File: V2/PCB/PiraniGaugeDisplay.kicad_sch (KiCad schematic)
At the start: 70 parts, among them J101 AuxIN, J102 Conn_02x03_Odd_Even, J103 RJ45, U101 AMS1117-3.3, U102 SN75176AD, U103 LM2596S-5, U104 ESP32-S3-WROOM-1(N16R2)

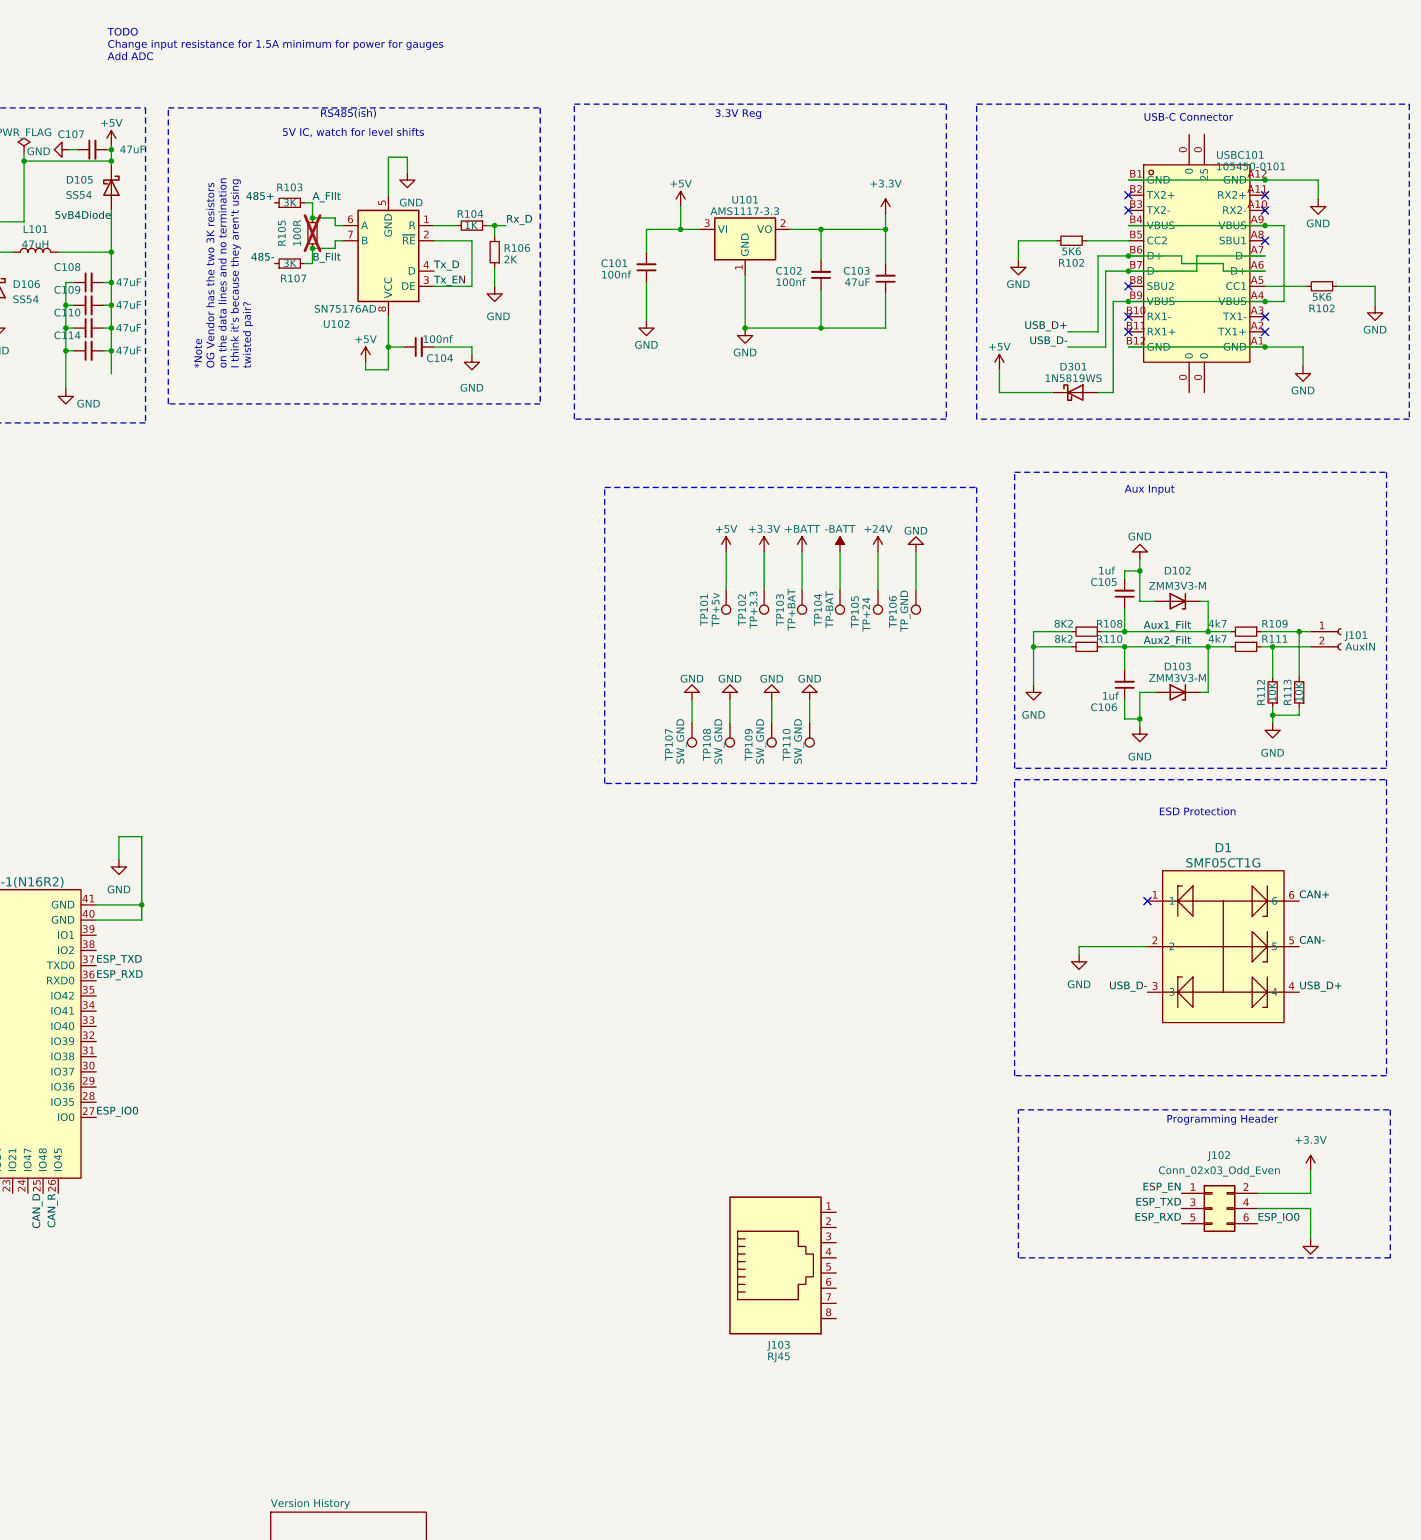
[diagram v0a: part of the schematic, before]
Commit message: Added buttons
Added boot/reset buttons to PCB
Should probably add some extras just for future expansion
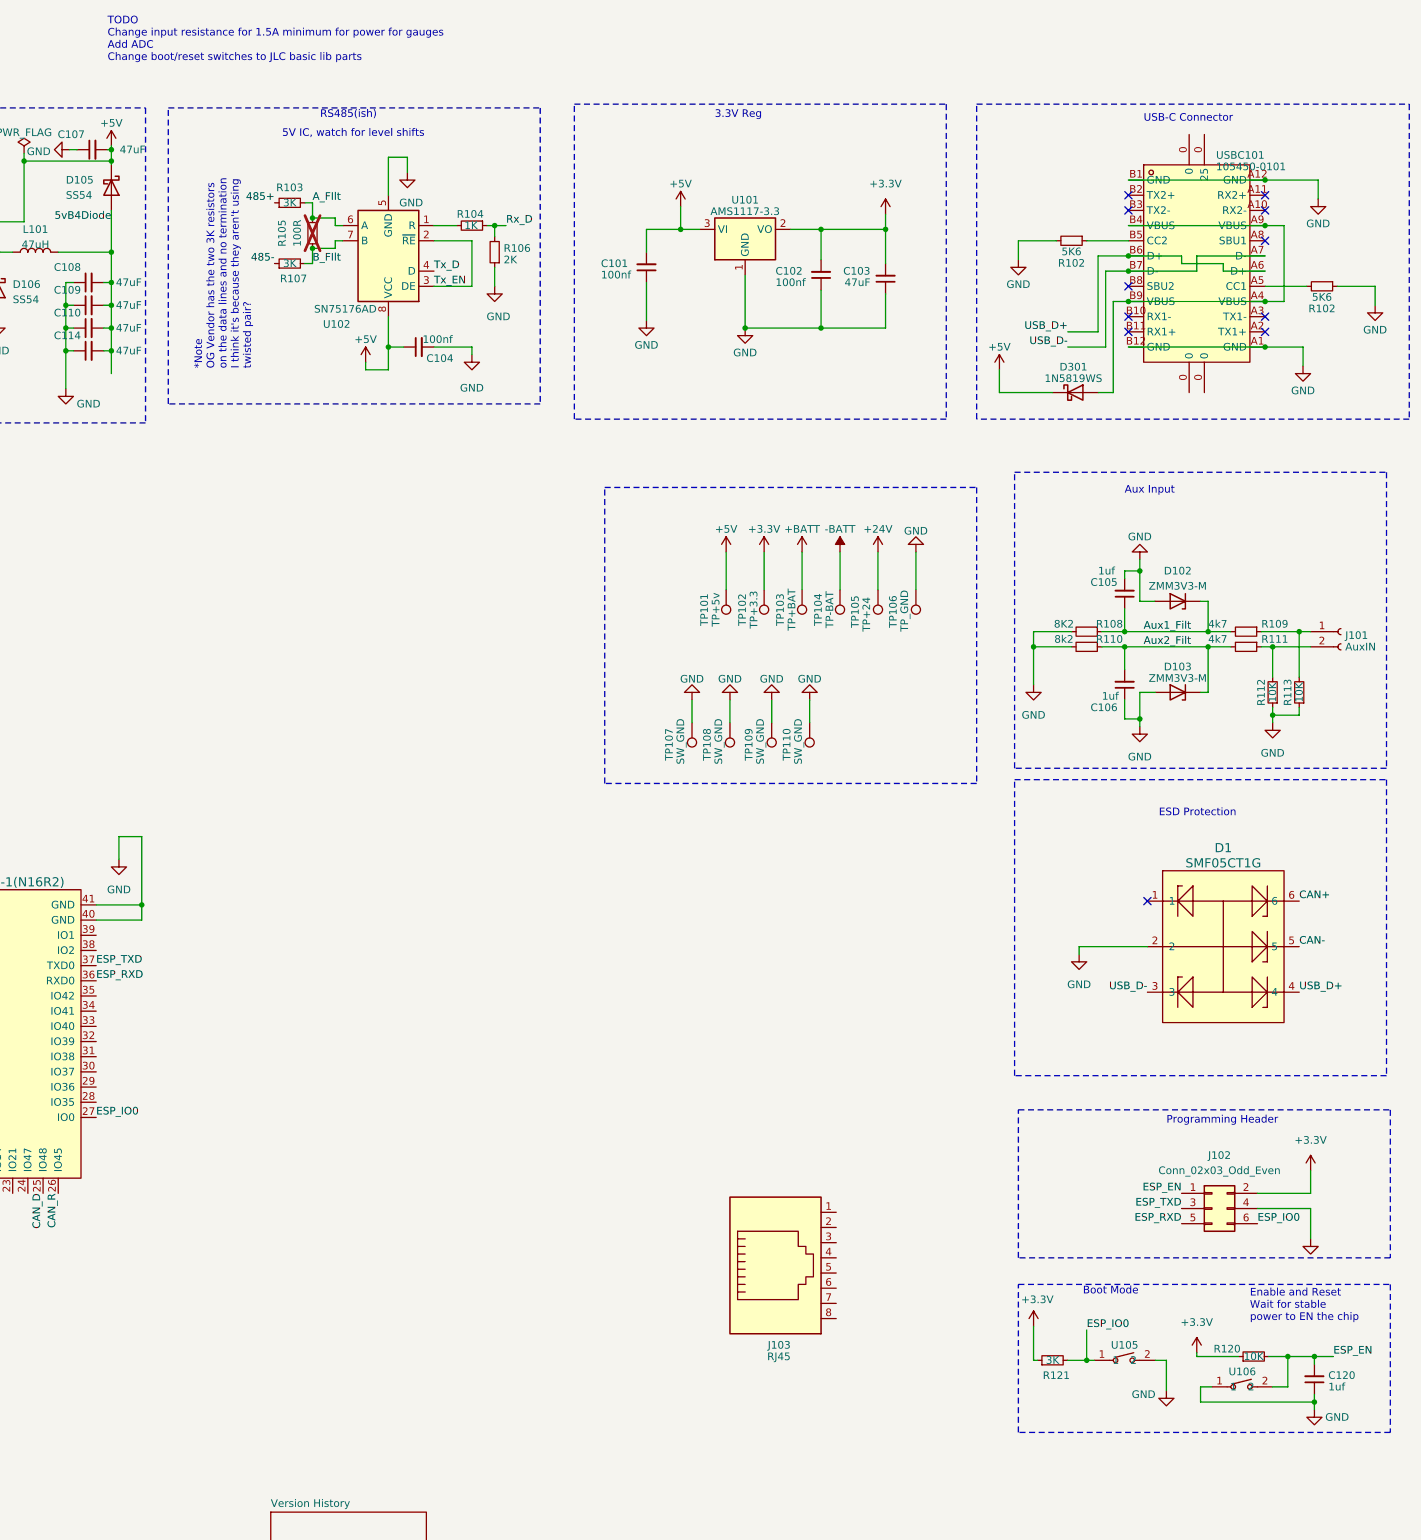
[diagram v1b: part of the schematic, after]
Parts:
- added C120: 1uf, Capacitor_SMD:C_0805_2012Metric, symbol Device:C_Small
- added R120: 10K, Resistor_SMD:R_0805_2012Metric, symbol Device:R_Small
- added R121: 3K, Resistor_SMD:R_0805_2012Metric, symbol Device:R_Small
- added U105, U106: SW-SMD_L6.1-W3.5-LS8.0, easyeda2kicad:SW-SMD_L6.1-W3.5-LS8.0, symbol easyeda2kicad:GT-TC060A-H025-L1
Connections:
- net +3.3V: now also R120.1, R121.1
- net ESP_EN: now also C120.2, R120.2, U106.2
- net ESP_IO0: now also R121.2, U105.1
- net GND: now also C120.1, U105.2, U106.1
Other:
- note added: "Boot Mode"
- note added: "Enable and Reset Wait for stable power to EN the chip"
- note added: "TODO Change input resistance for 1.5A minimum for power for gauges Add ADC Change boot/reset switches to JLC basic lib parts"
- note removed: "TODO Change input resistance for 1.5A minimum for power for gauges Add ADC"
